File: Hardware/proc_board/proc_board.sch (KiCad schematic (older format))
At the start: 11 parts, among them J1 Conn_01x40, U1 GAL16V8, U2 W65C02SxP, U3 HM62256BLP, U4 28C256

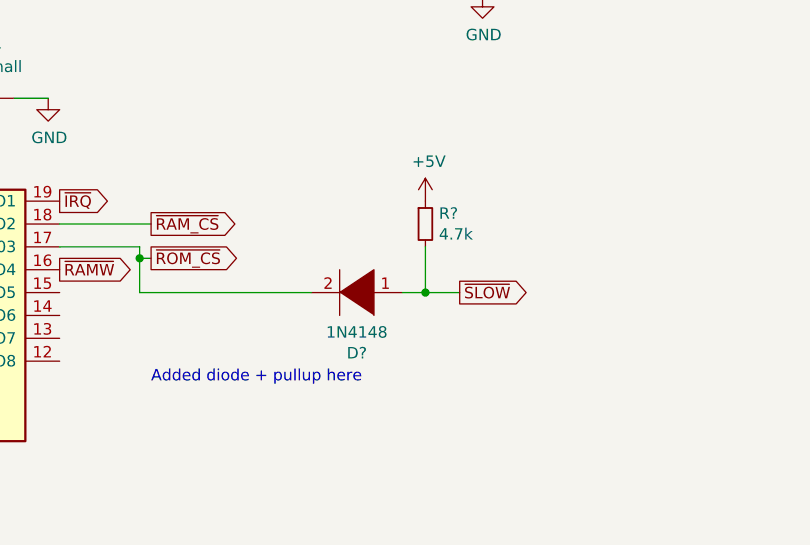
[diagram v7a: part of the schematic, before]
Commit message: Update processor board according to schematic
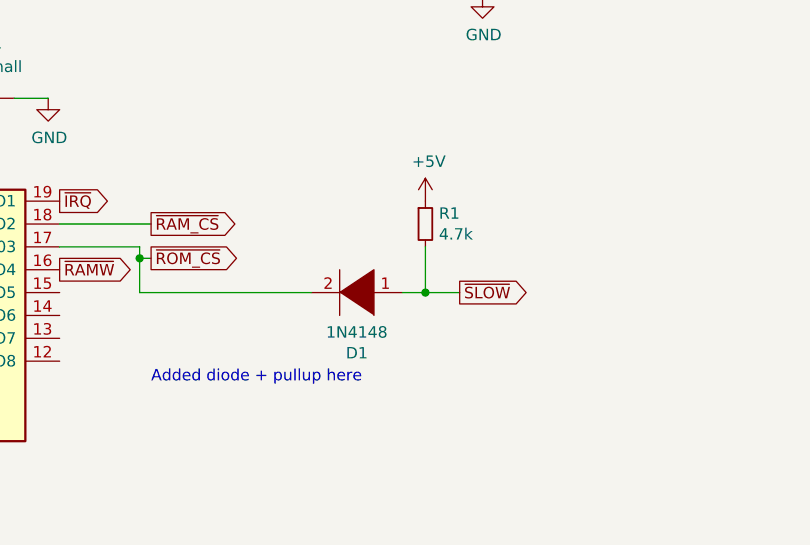
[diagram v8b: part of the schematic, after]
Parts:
- gave numbers to parts that had none: 2
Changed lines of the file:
@@
 Added diode + pullup here
 $Comp
-L pspice:DIODE D?
+L pspice:DIODE D1
 U 1 1 60359E86
 P 4050 6350
-F 0 "D?" H 4050 6615 50  0000 C CNN
+F 0 "D1" H 4050 6615 50  0000 C CNN
 F 1 "1N4148" H 4050 6524 50  0000 C CNN
 F 2 "Diode_THT:D_DO-35_SOD27_P7.62mm_Horizontal" H 4050 6350 50  0001 C CNN
@@
 	3100 6350 3850 6350
 $Comp
-L Device:R_Small R?
+L Device:R_Small R1
 U 1 1 6035C6C6
 P 4350 6050
-F 0 "R?" H 4409 6096 50  0000 L CNN
+F 0 "R1" H 4409 6096 50  0000 L CNN
 F 1 "4.7k" H 4409 6005 50  0000 L CNN
 F 2 "Resistor_SMD:R_0805_2012Metric_Pad1.15x1.40mm_HandSolder" H 4350 6050 50  0001 C CNN
@@
 $EndComp
 $Comp
-L power:+5V #PWR?
+L power:+5V #PWR0113
 U 1 1 6035CE86
 P 4350 5950
-F 0 "#PWR?" H 4350 5800 50  0001 C CNN
+F 0 "#PWR0113" H 4350 5800 50  0001 C CNN
 F 1 "+5V" H 4365 6123 50  0000 C CNN
 F 2 "" H 4350 5950 50  0001 C CNN
